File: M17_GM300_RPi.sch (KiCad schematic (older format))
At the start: 35 parts, among them J1 RJ45, J2 SJ1-3523N, J3 1935161, J4 DB9_Female, J5 RPi Header, Q1 2N7000, Q2 2N7000, Q3 2N7000, Q4 2N7000, SW1 SW_Push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

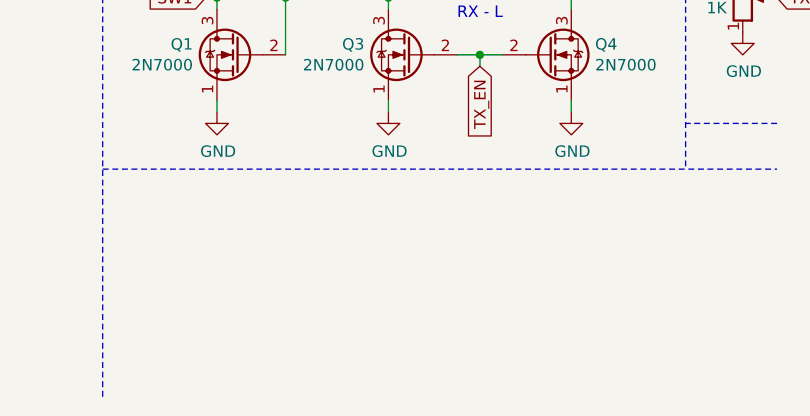
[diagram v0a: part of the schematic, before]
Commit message: increased passives to 0805. preliminary layout.
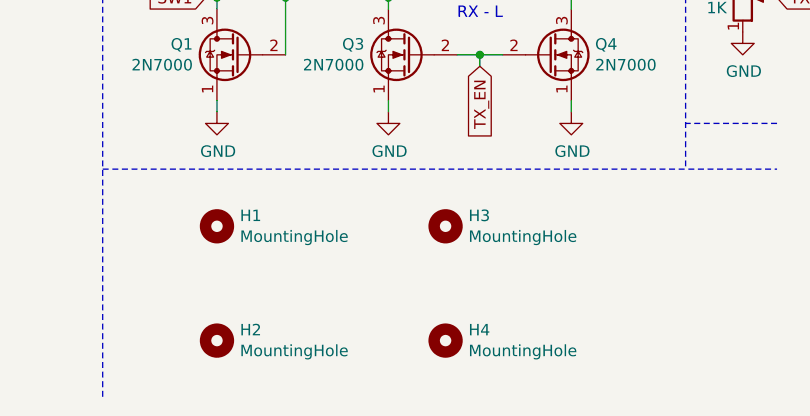
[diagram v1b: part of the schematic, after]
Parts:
- added H1, H2, H3, H4: MountingHole, MountingHole:MountingHole_2.7mm_M2.5, symbol Mechanical:MountingHole
- C1, C2: footprint Capacitor_SMD:C_0603_1608Metric -> Capacitor_SMD:C_1206_3216Metric_Pad1.33x1.80mm_HandSolder
- C3, C4, C5, C6, C7: footprint Capacitor_SMD:C_0603_1608Metric -> Capacitor_SMD:C_0805_2012Metric_Pad1.18x1.45mm_HandSolder
- D2: footprint (none) -> Diode_SMD:D_SOD-323F
- D3, D4, D5: footprint LED_SMD:LED_0603_1608Metric -> LED_SMD:LED_0805_2012Metric_Pad1.15x1.40mm_HandSolder
- R1, R2, R3, R4, R5, R6, R7, R8, R9: footprint Resistor_SMD:R_0603_1608Metric -> Resistor_SMD:R_0805_2012Metric_Pad1.20x1.40mm_HandSolder
- RV1, RV2: footprint (none) -> Potentiometer_SMD:Potentiometer_Bourns_3361P_Vertical
- SW1: footprint (none) -> Button_Switch_SMD:SW_SPST_B3U-1000P
- U2: footprint Package_SO:SOIC-16_3.9x9.9mm_P1.27mm -> Package_SO:SOIC-14_3.9x8.7mm_P1.27mm
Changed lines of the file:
@@
 F 0 "D5" V 9189 1432 50  0000 R CNN
 F 1 "GRN" V 9098 1432 50  0000 R CNN
-F 2 "LED_SMD:LED_0603_1608Metric" H 9150 1550 50  0001 C CNN
+F 2 "LED_SMD:LED_0805_2012Metric_Pad1.15x1.40mm_HandSolder" H 9150 1550 50  0001 C CNN
 F 3 "~" H 9150 1550 50  0001 C CNN
 	1    9150 1550
@@
 F 0 "D4" V 8839 1432 50  0000 R CNN
 F 1 "RED" V 8748 1432 50  0000 R CNN
-F 2 "LED_SMD:LED_0603_1608Metric" H 8800 1550 50  0001 C CNN
+F 2 "LED_SMD:LED_0805_2012Metric_Pad1.15x1.40mm_HandSolder" H 8800 1550 50  0001 C CNN
 F 3 "~" H 8800 1550 50  0001 C CNN
 	1    8800 1550
@@
 F 0 "D3" V 8489 1432 50  0000 R CNN
 F 1 "BLU" V 8398 1432 50  0000 R CNN
-F 2 "LED_SMD:LED_0603_1608Metric" H 8450 1550 50  0001 C CNN
+F 2 "LED_SMD:LED_0805_2012Metric_Pad1.15x1.40mm_HandSolder" H 8450 1550 50  0001 C CNN
 F 3 "~" H 8450 1550 50  0001 C CNN
 	1    8450 1550
@@
 F 0 "R8" H 9220 2046 50  0000 L CNN
 F 1 "2K2" H 9220 1955 50  0000 L CNN
-F 2 "Resistor_SMD:R_0603_1608Metric" V 9080 2000 50  0001 C CNN
+F 2 "Resistor_SMD:R_0805_2012Metric_Pad1.20x1.40mm_HandSolder" V 9080 2000 50  0001 C CNN
 F 3 "~" H 9150 2000 50  0001 C CNN
 	1    9150 2000
@@
 F 0 "R7" H 8870 2046 50  0000 L CNN
 F 1 "1K" H 8870 1955 50  0000 L CNN
-F 2 "Resistor_SMD:R_0603_1608Metric" V 8730 2000 50  0001 C CNN
+F 2 "Resistor_SMD:R_0805_2012Metric_Pad1.20x1.40mm_HandSolder" V 8730 2000 50  0001 C CNN
 F 3 "~" H 8800 2000 50  0001 C CNN
 	1    8800 2000
@@
 F 0 "R6" H 8520 2046 50  0000 L CNN
 F 1 "2K2" H 8520 1955 50  0000 L CNN
-F 2 "Resistor_SMD:R_0603_1608Metric" V 8380 2000 50  0001 C CNN
+F 2 "Resistor_SMD:R_0805_2012Metric_Pad1.20x1.40mm_HandSolder" V 8380 2000 50  0001 C CNN
 F 3 "~" H 8450 2000 50  0001 C CNN
 	1    8450 2000
@@
 F 0 "R3" H 5920 1746 50  0000 L CNN
 F 1 "390R" H 5920 1655 50  0000 L CNN
-F 2 "Resistor_SMD:R_0603_1608Metric" V 5780 1700 50  0001 C CNN
+F 2 "Resistor_SMD:R_0805_2012Metric_Pad1.20x1.40mm_HandSolder" V 5780 1700 50  0001 C CNN
 F 3 "~" H 5850 1700 50  0001 C CNN
 	1    5850 1700
@@
 F 0 "R4" V 5893 1300 50  0000 C CNN
 F 1 "680R" V 5984 1300 50  0000 C CNN
-F 2 "Resistor_SMD:R_0603_1608Metric" V 6030 1300 50  0001 C CNN
+F 2 "Resistor_SMD:R_0805_2012Metric_Pad1.20x1.40mm_HandSolder" V 6030 1300 50  0001 C CNN
 F 3 "~" H 6100 1300 50  0001 C CNN
 	1    6100 1300
@@
 F 0 "C3" V 5345 1300 50  0000 C CNN
 F 1 "22u" V 5436 1300 50  0000 C CNN
-F 2 "Capacitor_SMD:C_0603_1608Metric" H 5638 1150 50  0001 C CNN
+F 2 "Capacitor_SMD:C_0805_2012Metric_Pad1.18x1.45mm_HandSolder" H 5638 1150 50  0001 C CNN
 F 3 "~" H 5600 1300 50  0001 C CNN
 	1    5600 1300
@@
 F 0 "U2" H 8850 3435 50  0000 C CNN
 F 1 "4066" H 8850 3526 50  0000 C CNN
-F 2 "Package_SO:SOIC-16_3.9x9.9mm_P1.27mm" H 8850 3700 50  0001 C CNN
+F 2 "Package_SO:SOIC-14_3.9x8.7mm_P1.27mm" H 8850 3700 50  0001 C CNN
 F 3 "http://www.ti.com/lit/ds/symlink/cd4066b.pdf" H 8850 3700 50  0001 C CNN
 	1    8850 3700
@@
 F 0 "U2" H 8850 4327 50  0000 C CNN
 F 1 "4066" H 8850 4236 50  0000 C CNN
-F 2 "Package_SO:SOIC-16_3.9x9.9mm_P1.27mm" H 8850 4500 50  0001 C CNN
+F 2 "Package_SO:SOIC-14_3.9x8.7mm_P1.27mm" H 8850 4500 50  0001 C CNN
 F 3 "http://www.ti.com/lit/ds/symlink/cd4066b.pdf" H 8850 4500 50  0001 C CNN
 	4    8850 4500
@@
 F 0 "U2" H 9700 3035 50  0000 C CNN
 F 1 "4066" H 9700 3126 50  0000 C CNN
-F 2 "Package_SO:SOIC-16_3.9x9.9mm_P1.27mm" H 9700 3300 50  0001 C CNN
+F 2 "Package_SO:SOIC-14_3.9x8.7mm_P1.27mm" H 9700 3300 50  0001 C CNN
 F 3 "http://www.ti.com/lit/ds/symlink/cd4066b.pdf" H 9700 3300 50  0001 C CNN
 	3    9700 3300
@@
 F 0 "U2" H 9700 4677 50  0000 C CNN
 F 1 "4066" H 9700 4586 50  0000 C CNN
-F 2 "Package_SO:SOIC-16_3.9x9.9mm_P1.27mm" H 9700 4850 50  0001 C CNN
+F 2 "Package_SO:SOIC-14_3.9x8.7mm_P1.27mm" H 9700 4850 50  0001 C CNN
 F 3 "http://www.ti.com/lit/ds/symlink/cd4066b.pdf" H 9700 4850 50  0001 C CNN
 	2    9700 4850
@@
 F 0 "C4" H 8515 4146 50  0000 L CNN
 F 1 "220n" H 8515 4055 50  0000 L CNN
-F 2 "Capacitor_SMD:C_0603_1608Metric" H 8438 3950 50  0001 C CNN
+F 2 "Capacitor_SMD:C_0805_2012Metric_Pad1.18x1.45mm_HandSolder" H 8438 3950 50  0001 C CNN
 F 3 "~" H 8400 4100 50  0001 C CNN
 	1    8400 4100
@@
 F 0 "D2" V 7754 4130 50  0000 L CNN
 F 1 "2V7" V 7845 4130 50  0000 L CNN
-F 2 "" H 7800 4050 50  0001 C CNN
+F 2 "Diode_SMD:D_SOD-323F" H 7800 4050 50  0001 C CNN
 F 3 "~" H 7800 4050 50  0001 C CNN
 	1    7800 4050
@@
 F 0 "U2" H 10980 4146 50  0000 L CNN
 F 1 "4066" H 10980 4055 50  0000 L CNN
-F 2 "Package_SO:SOIC-16_3.9x9.9mm_P1.27mm" H 10750 4100 50  0001 C CNN
+F 2 "Package_SO:SOIC-14_3.9x8.7mm_P1.27mm" H 10750 4100 50  0001 C CNN
 F 3 "http://www.ti.com/lit/ds/symlink/cd4066b.pdf" H 10750 4100 50  0001 C CNN
 	5    10750 4100
@@
 F 0 "C7" H 10368 4146 50  0000 L CNN
 F 1 "47u" H 10368 4055 50  0000 L CNN
-F 2 "Capacitor_SMD:C_0603_1608Metric" H 10288 3950 50  0001 C CNN
+F 2 "Capacitor_SMD:C_0805_2012Metric_Pad1.18x1.45mm_HandSolder" H 10288 3950 50  0001 C CNN
 F 3 "~" H 10250 4100 50  0001 C CNN
 	1    10250 4100
@@
 F 0 "SW1" V 10504 6248 50  0000 L CNN
 F 1 "SW_Push" V 10595 6248 50  0000 L CNN
-F 2 "" H 10550 6300 50  0001 C CNN
+F 2 "Button_Switch_SMD:SW_SPST_B3U-1000P" H 10550 6300 50  0001 C CNN
 F 3 "~" H 10550 6300 50  0001 C CNN
 	1    10550 6100
@@
 F 0 "R9" H 10620 5696 50  0000 L CNN
 F 1 "22K" H 10620 5605 50  0000 L CNN
-F 2 "Resistor_SMD:R_0603_1608Metric" V 10480 5650 50  0001 C CNN
+F 2 "Resistor_SMD:R_0805_2012Metric_Pad1.20x1.40mm_HandSolder" V 10480 5650 50  0001 C CNN
 F 3 "~" H 10550 5650 50  0001 C CNN
 	1    10550 5650
@@
 F 0 "C6" V 9755 5900 50  0000 C CNN
 F 1 "220u" V 9664 5900 50  0000 C CNN
-F 2 "Capacitor_SMD:C_0603_1608Metric" H 9538 5750 50  0001 C CNN
+F 2 "Capacitor_SMD:C_0805_2012Metric_Pad1.18x1.45mm_HandSolder" H 9538 5750 50  0001 C CNN
 F 3 "~" H 9500 5900 50  0001 C CNN
 	1    9500 5900
@@
 F 0 "C5" V 8248 5800 50  0000 C CNN
 F 1 "470n" V 8339 5800 50  0000 C CNN
-F 2 "Capacitor_SMD:C_0603_1608Metric" H 8538 5650 50  0001 C CNN
+F 2 "Capacitor_SMD:C_0805_2012Metric_Pad1.18x1.45mm_HandSolder" H 8538 5650 50  0001 C CNN
 F 3 "~" H 8500 5800 50  0001 C CNN
 	1    8500 5800
@@
 F 0 "RV2" H 8081 5754 50  0000 R CNN
 F 1 "4K7" H 8081 5845 50  0000 R CNN
-F 2 "" H 8150 5800 50  0001 C CNN
+F 2 "Potentiometer_SMD:Potentiometer_Bourns_3361P_Vertical" H 8150 5800 50  0001 C CNN
 F 3 "~" H 8150 5800 50  0001 C CNN
 	1    8150 5800
@@
 F 0 "R5" V 7743 5550 50  0000 C CNN
 F 1 "39K" V 7834 5550 50  0000 C CNN
-F 2 "Resistor_SMD:R_0603_1608Metric" V 7880 5550 50  0001 C CNN
+F 2 "Resistor_SMD:R_0805_2012Metric_Pad1.20x1.40mm_HandSolder" V 7880 5550 50  0001 C CNN
 F 3 "~" H 7950 5550 50  0001 C CNN
 	1    7950 5550
@@
 F 0 "RV1" H 6730 5954 50  0000 R CNN
 F 1 "1K" H 6730 6045 50  0000 R CNN
-F 2 "" H 6800 6000 50  0001 C CNN
+F 2 "Potentiometer_SMD:Potentiometer_Bourns_3361P_Vertical" H 6800 6000 50  0001 C CNN
 F 3 "~" H 6800 6000 50  0001 C CNN
 	1    6800 6000
@@
 F 0 "R1" H 4570 5846 50  0000 L CNN
 F 1 "47K" H 4570 5755 50  0000 L CNN
-F 2 "Resistor_SMD:R_0603_1608Metric" V 4430 5800 50  0001 C CNN
+F 2 "Resistor_SMD:R_0805_2012Metric_Pad1.20x1.40mm_HandSolder" V 4430 5800 50  0001 C CNN
 F 3 "~" H 4500 5800 50  0001 C CNN
 	1    4500 5800
@@
 F 0 "R2" H 5320 5846 50  0000 L CNN
 F 1 "47K" H 5320 5755 50  0000 L CNN
-F 2 "Resistor_SMD:R_0603_1608Metric" V 5180 5800 50  0001 C CNN
+F 2 "Resistor_SMD:R_0805_2012Metric_Pad1.20x1.40mm_HandSolder" V 5180 5800 50  0001 C CNN
 F 3 "~" H 5250 5800 50  0001 C CNN
 	1    5250 5800
@@
 F 0 "C1" H 2068 1896 50  0000 L CNN
 F 1 "1000 uF" H 2068 1805 50  0000 L CNN
-F 2 "Capacitor_SMD:C_0603_1608Metric" H 1988 1700 50  0001 C CNN
+F 2 "Capacitor_SMD:C_1206_3216Metric_Pad1.33x1.80mm_HandSolder" H 1988 1700 50  0001 C CNN
 F 3 "~" H 1950 1850 50  0001 C CNN
 	1    1950 1850
@@
 F 0 "C2" H 3268 1896 50  0000 L CNN
 F 1 "1000 uF" H 3268 1805 50  0000 L CNN
-F 2 "Capacitor_SMD:C_0603_1608Metric" H 3188 1700 50  0001 C CNN
+F 2 "Capacitor_SMD:C_1206_3216Metric_Pad1.33x1.80mm_HandSolder" H 3188 1700 50  0001 C CNN
 F 3 "~" H 3150 1850 50  0001 C CNN
 	1    3150 1850
@@
 Wire Wire Line
 	3150 1400 3150 1200
+$Comp
+L Mechanical:MountingHole H1
+U 1 1 607A7869
+P 4500 7000
+F 0 "H1" H 4600 7046 50  0000 L CNN
+F 1 "MountingHole" H 4600 6955 50  0000 L CNN
+F 2 "MountingHole:MountingHole_2.7mm_M2.5" H 4500 7000 50  0001 C CNN
+F 3 "~" H 4500 7000 50  0001 C CNN
+	1    4500 7000
+	1    0    0    -1
+$EndComp
+$Comp
+L Mechanical:MountingHole H2
+U 1 1 607A87E8
+P 4500 7500
+F 0 "H2" H 4600 7546 50  0000 L CNN
+F 1 "MountingHole" H 4600 7455 50  0000 L CNN
+F 2 "MountingHole:MountingHole_2.7mm_M2.5" H 4500 7500 50  0001 C CNN
+F 3 "~" H 4500 7500 50  0001 C CNN
+	1    4500 7500
+	1    0    0    -1
+$EndComp
+$Comp
+L Mechanical:MountingHole H4
+U 1 1 607A93B8
+P 5500 7500
+F 0 "H4" H 5600 7546 50  0000 L CNN
+F 1 "MountingHole" H 5600 7455 50  0000 L CNN
+F 2 "MountingHole:MountingHole_2.7mm_M2.5" H 5500 7500 50  0001 C CNN
+F 3 "~" H 5500 7500 50  0001 C CNN
+	1    5500 7500
+	1    0    0    -1
+$EndComp
+$Comp
+L Mechanical:MountingHole H3
+U 1 1 607AA0EA
+P 5500 7000
+F 0 "H3" H 5600 7046 50  0000 L CNN
+F 1 "MountingHole" H 5600 6955 50  0000 L CNN
+F 2 "MountingHole:MountingHole_2.7mm_M2.5" H 5500 7000 50  0001 C CNN
+F 3 "~" H 5500 7000 50  0001 C CNN
+	1    5500 7000
+	1    0    0    -1
+$EndComp
 $EndSCHEMATC

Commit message: updated layout to proposed final
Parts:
- U3: footprint Package_SO:MSOP-8_3x3mm_P0.65mm -> Package_SO:SOIC-8_3.9x4.9mm_P1.27mm
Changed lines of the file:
@@
 F 0 "U3" H 9050 6100 50  0000 L CNN
 F 1 "LM386" H 9050 6000 50  0000 L CNN
-F 2 "Package_SO:MSOP-8_3x3mm_P0.65mm" H 9050 6000 50  0001 C CNN
+F 2 "Package_SO:SOIC-8_3.9x4.9mm_P1.27mm" H 9050 6000 50  0001 C CNN
 F 3 "http://www.ti.com/lit/ds/symlink/lm386.pdf" H 9150 6100 50  0001 C CNN
 	1    8950 5900

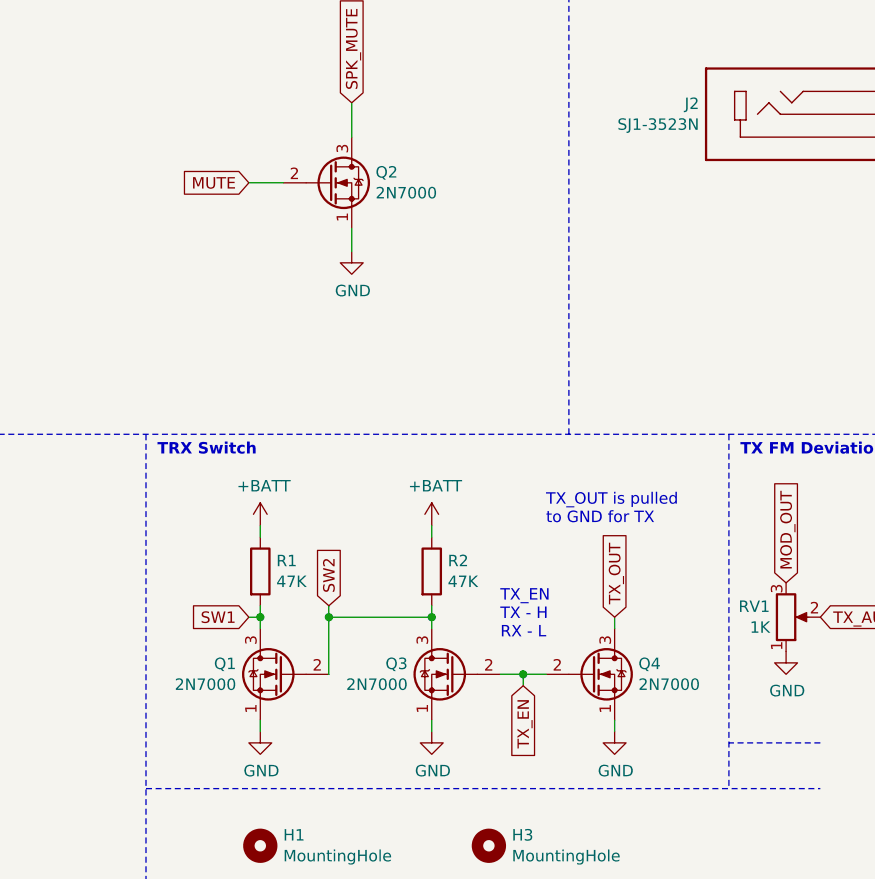
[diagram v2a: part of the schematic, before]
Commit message: part and footprint updates, routing
updated parts and footprints for header and transistors. updated layout. most routing is complete pending changes to schematic.
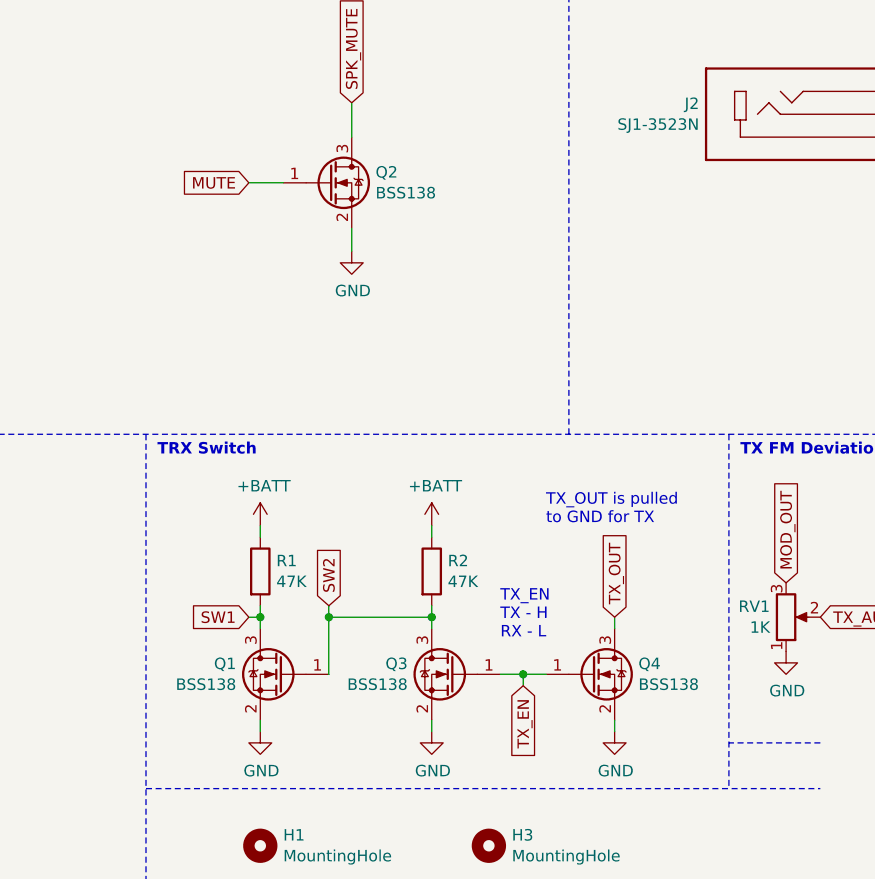
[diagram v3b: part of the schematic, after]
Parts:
- removed Q1, Q2, Q3, Q4: 2N7000, Package_TO_SOT_SMD:SOT-23, symbol Transistor_FET:2N7000
- added Q1, Q2, Q3, Q4: BSS138, Package_TO_SOT_SMD:SOT-23, symbol Transistor_FET:BSS138
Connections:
- net GND: now also Q1.2 (S), Q2.2 (S), Q3.2 (S), Q4.2 (S)
- net MUTE: now also Q2.1 (G)
- net SPK_MUTE: now also Q2.3 (D)
- net SW1: now also Q1.3 (D)
- net SW2: now also Q1.1 (G), Q3.3 (D)
- net TX_EN: now also Q3.1 (G), Q4.1 (G)
- net TX_OUT: now also Q4.3 (D)
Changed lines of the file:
@@
 Text Notes 6600 5300 0    50   ~ 10
 TX FM Deviation
-$Comp
-L Transistor_FET:2N7000 Q1
-U 1 1 604E8D6A
-P 4600 6250
-F 0 "Q1" H 4805 6296 50  0000 L CNN
-F 1 "2N7000" H 4805 6205 50  0000 L CNN
-F 2 "Package_TO_SOT_SMD:SOT-23" H 4800 6175 50  0001 L CIN
-F 3 "https://www.onsemi.com/pub/Collateral/NDS7002A-D.PDF" H 4600 6250 50  0001 L CNN
-	1    4600 6250
-	-1   0    0    -1
-$EndComp
-$Comp
-L Transistor_FET:2N7000 Q3
-U 1 1 604E96EB
-P 5350 6250
-F 0 "Q3" H 5555 6296 50  0000 L CNN
-F 1 "2N7000" H 5555 6205 50  0000 L CNN
-F 2 "Package_TO_SOT_SMD:SOT-23" H 5550 6175 50  0001 L CIN
-F 3 "https://www.onsemi.com/pub/Collateral/NDS7002A-D.PDF" H 5350 6250 50  0001 L CNN
-	1    5350 6250
-	-1   0    0    -1
-$EndComp
-$Comp
-L Transistor_FET:2N7000 Q4
-U 1 1 604E9D84
-P 5950 6250
-F 0 "Q4" H 6154 6296 50  0000 L CNN
-F 1 "2N7000" H 6154 6205 50  0000 L CNN
-F 2 "Package_TO_SOT_SMD:SOT-23" H 6150 6175 50  0001 L CIN
-F 3 "https://www.onsemi.com/pub/Collateral/NDS7002A-D.PDF" H 5950 6250 50  0001 L CNN
-	1    5950 6250
-	1    0    0    -1
-$EndComp
 Wire Wire Line
 	5550 6250 5650 6250
@@
 Wire Wire Line
 	8150 3700 8550 3700
-$Comp
-L Transistor_FET:2N7000 Q2
-U 1 1 6059E86D
-P 4800 4100
-F 0 "Q2" H 5004 4146 50  0000 L CNN
-F 1 "2N7000" H 5004 4055 50  0000 L CNN
-F 2 "Package_TO_SOT_SMD:SOT-23" H 5000 4025 50  0001 L CIN
-F 3 "https://www.onsemi.com/pub/Collateral/NDS7002A-D.PDF" H 4800 4100 50  0001 L CNN
-	1    4800 4100
-	1    0    0    -1
-$EndComp
 Wire Wire Line
 	4450 4100 4600 4100
@@
 	1    0    0    -1
 $EndComp
+$Comp
+L Transistor_FET:BSS138 Q1
+U 1 1 60781DCA
+P 4600 6250
+F 0 "Q1" H 4805 6296 50  0000 L CNN
+F 1 "BSS138" H 4805 6205 50  0000 L CNN
+F 2 "Package_TO_SOT_SMD:SOT-23" H 4800 6175 50  0001 L CIN
+F 3 "https://www.onsemi.com/pub/Collateral/BSS138-D.PDF" H 4600 6250 50  0001 L CNN
+	1    4600 6250
+	-1   0    0    -1
+$EndComp
+$Comp
+L Transistor_FET:BSS138 Q3
+U 1 1 607891AA
+P 5350 6250
+F 0 "Q3" H 5555 6296 50  0000 L CNN
+F 1 "BSS138" H 5555 6205 50  0000 L CNN
+F 2 "Package_TO_SOT_SMD:SOT-23" H 5550 6175 50  0001 L CIN
+F 3 "https://www.onsemi.com/pub/Collateral/BSS138-D.PDF" H 5350 6250 50  0001 L CNN
+	1    5350 6250
+	-1   0    0    -1
+$EndComp
+$Comp
+L Transistor_FET:BSS138 Q4
+U 1 1 6078B94D
+P 5950 6250
+F 0 "Q4" H 6154 6296 50  0000 L CNN
+F 1 "BSS138" H 6154 6205 50  0000 L CNN
+F 2 "Package_TO_SOT_SMD:SOT-23" H 6150 6175 50  0001 L CIN
+F 3 "https://www.onsemi.com/pub/Collateral/BSS138-D.PDF" H 5950 6250 50  0001 L CNN
+	1    5950 6250
+	1    0    0    -1
+$EndComp
+$Comp
+L Transistor_FET:BSS138 Q2
+U 1 1 607C75A9
+P 4800 4100
+F 0 "Q2" H 5004 4146 50  0000 L CNN
+F 1 "BSS138" H 5004 4055 50  0000 L CNN
+F 2 "Package_TO_SOT_SMD:SOT-23" H 5000 4025 50  0001 L CIN
+F 3 "https://www.onsemi.com/pub/Collateral/BSS138-D.PDF" H 4800 4100 50  0001 L CNN
+	1    4800 4100
+	1    0    0    -1
+$EndComp

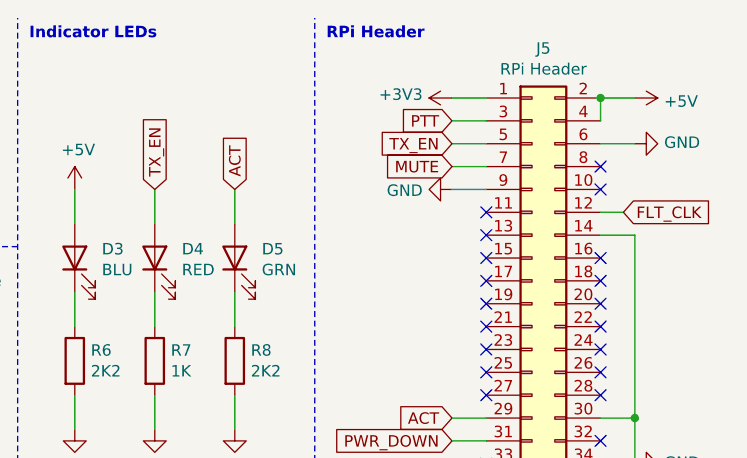
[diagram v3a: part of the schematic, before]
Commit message: put pin 17 on 3v3
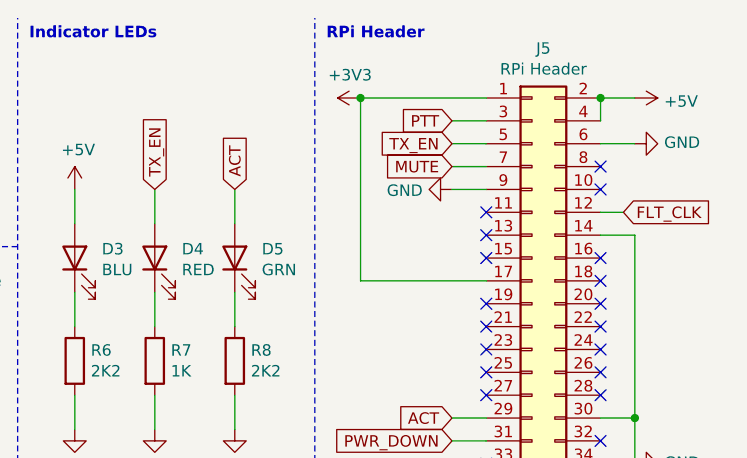
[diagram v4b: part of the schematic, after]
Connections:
- net +3V3: now also J5.17 (Pin_17)
- no-connect marks 36 -> 35
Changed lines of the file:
@@
 L power:+3V3 #PWR028
 U 1 1 603AED58
-P 10100 850
-F 0 "#PWR028" H 10100 700 50  0001 C CNN
-F 1 "+3V3" V 10115 978 50  0000 L CNN
-F 2 "" H 10100 850 50  0001 C CNN
-F 3 "" H 10100 850 50  0001 C CNN
-	1    10100 850
+P 9700 850
+F 0 "#PWR028" H 9700 700 50  0001 C CNN
+F 1 "+3V3" V 9800 800 50  0000 L CNN
+F 2 "" H 9700 850 50  0001 C CNN
+F 3 "" H 9700 850 50  0001 C CNN
+	1    9700 850
 	0    -1   -1   0
 $EndComp
@@
 Wire Wire Line
 	10250 1250 10100 1250
-Wire Wire Line
-	10250 850  10100 850
 Text GLabel 10100 950  0    50   Input ~ 0
 PTT
@@
 NoConn ~ 10250 1450
 NoConn ~ 10250 1550
-NoConn ~ 10250 1650
 NoConn ~ 10250 1750
 NoConn ~ 10250 1850
@@
 	1    0    0    -1
 $EndComp
+Wire Wire Line
+	9700 850  9700 1650
+Wire Wire Line
+	9700 1650 10250 1650
+Wire Wire Line
+	9700 850  10250 850
+Connection ~ 9700 850
 $EndSCHEMATC
